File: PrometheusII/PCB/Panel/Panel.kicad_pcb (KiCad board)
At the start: 2 copper layers, 40.3 x 128.5 mm, 4 parts

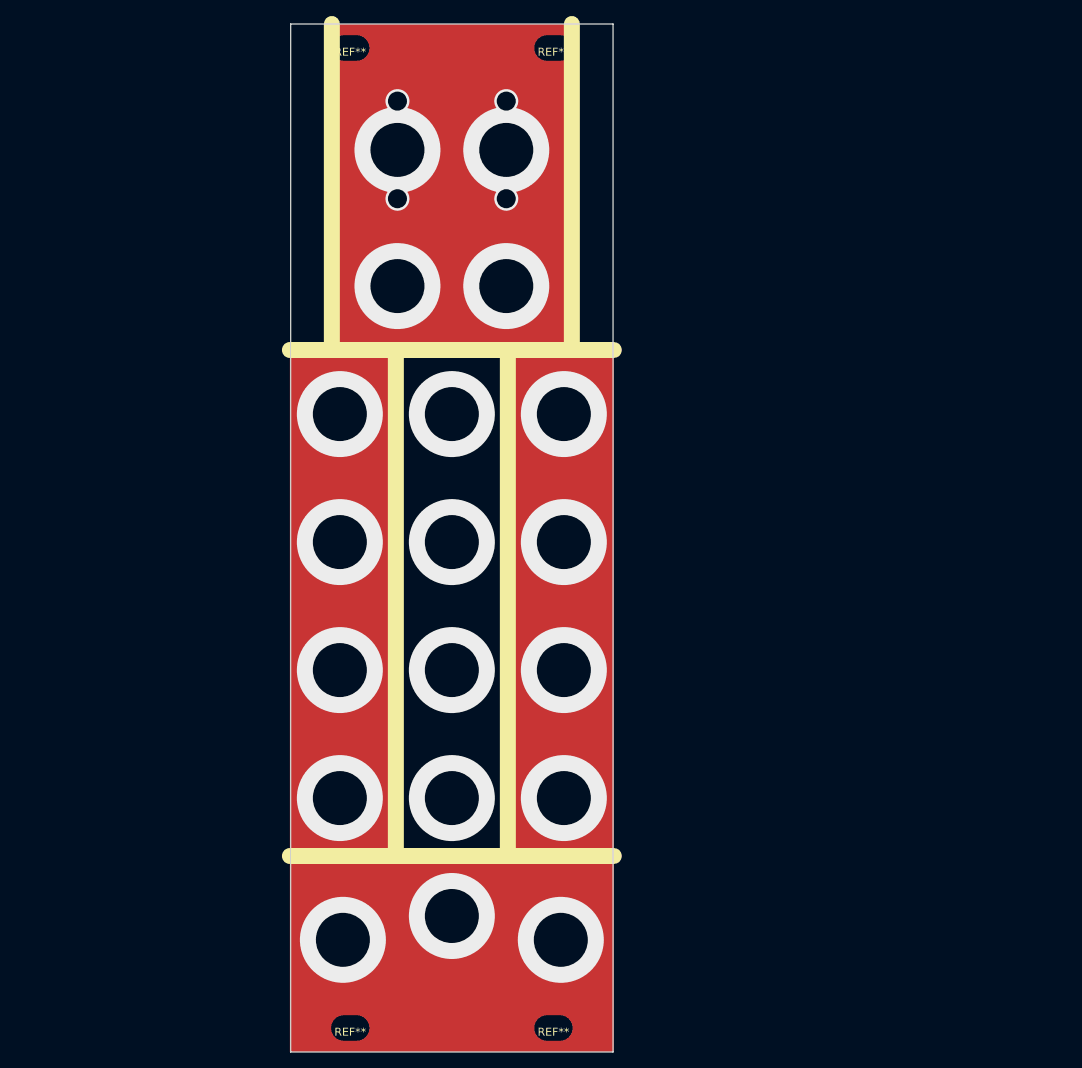
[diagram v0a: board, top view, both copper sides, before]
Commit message: Various DRC fixes
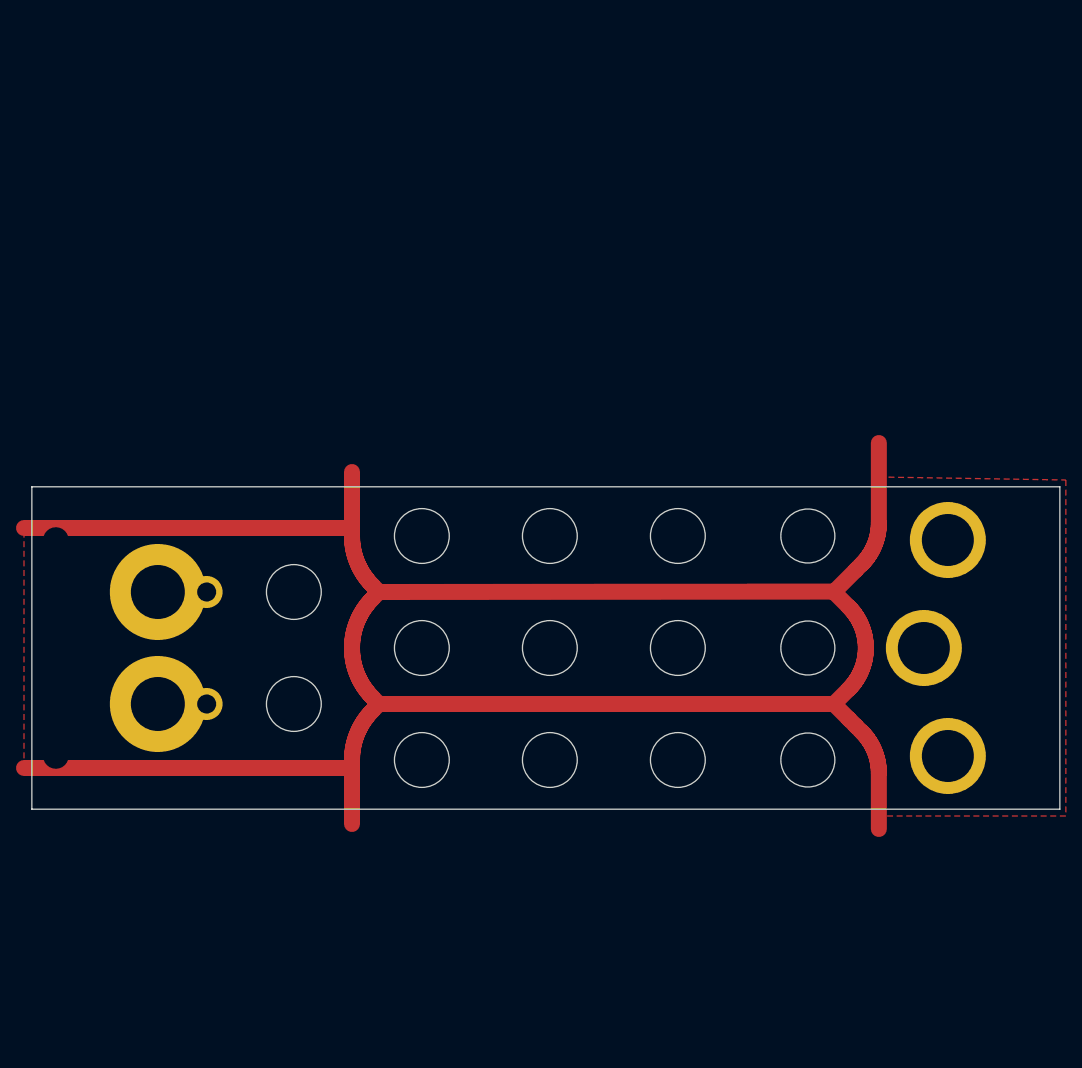
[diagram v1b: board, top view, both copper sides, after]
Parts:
- removed the REF** at (112.7, 24.5)
- removed the REF** at (87.3, 24.5)
- removed the REF** at (87.3, 147.0)
- removed the REF** at (112.7, 147.0)
- added G***: LOGO, ttt_lib:TTT_11.1x9.5, B.Cu at (74.5, 99.5)
- added REF**: PJ398SM_Plated, ttt_panels:PJ398SM_Plated, F.Cu at (162.0, 113.0)
- added REF**: Knob_Unplated, ttt_panels:Knob_Unplated, F.Cu at (112.2, 85.5)
- added REF**: Knob_Unplated, ttt_panels:Knob_Unplated, F.Cu at (112.2, 113.5)
- added REF**: Knob_Unplated, ttt_panels:Knob_Unplated, F.Cu at (112.2, 99.5)
- added REF**: Knob_Unplated, ttt_panels:Knob_Unplated, F.Cu at (96.2, 113.5)
- added REF**: Knob_Unplated, ttt_panels:Knob_Unplated, F.Cu at (96.2, 99.5)
- added REF**: Knob_Unplated, ttt_panels:Knob_Unplated, F.Cu at (80.2, 106.5)
- added REF**: Knob_Unplated, ttt_panels:Knob_Unplated, F.Cu at (80.2, 92.5)
- added REF**: Knob_Unplated, ttt_panels:Knob_Unplated, F.Cu at (96.2, 85.5)
- added REF**: Funswitch_Plated, ttt_panels:Funswitch_Plated, F.Cu at (63.2, 106.5)
- added REF**: Funswitch_Plated, ttt_panels:Funswitch_Plated, F.Cu at (63.2, 92.5)
- added REF**: PJ398SM_Unplated, ttt_panels:PJ398SM_Unplated, F.Cu at (144.5, 99.5)
- added REF**: euro_mounting_hole, ttt_lib:euro_mounting_hole, F.Cu at (173.0, 86.8)
- added REF**: euro_mounting_hole, ttt_lib:euro_mounting_hole, F.Cu at (173.0, 112.2)
- added REF**: euro_mounting_hole, ttt_lib:euro_mounting_hole, F.Cu at (50.5, 86.8)
- added REF**: PJ398SM_Plated, ttt_panels:PJ398SM_Plated, F.Cu at (162.0, 86.0)
- added REF**: euro_mounting_hole, ttt_lib:euro_mounting_hole, F.Cu at (50.5, 112.2)
- added REF**: PJ398SM_Unplated, ttt_panels:PJ398SM_Unplated, F.Cu at (144.5, 85.5)
- added REF**: Knob_Unplated, ttt_panels:Knob_Unplated, F.Cu at (128.2, 113.5)
- added REF**: Knob_Unplated, ttt_panels:Knob_Unplated, F.Cu at (128.2, 99.5)
- added REF**: Knob_Unplated, ttt_panels:Knob_Unplated, F.Cu at (128.2, 85.5)
- added REF**: PJ398SM_Unplated, ttt_panels:PJ398SM_Unplated, F.Cu at (144.5, 113.5)
- added REF**: PJ398SM_Plated, ttt_panels:PJ398SM_Plated, F.Cu at (159.0, 99.5)
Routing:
- net (no net): track 0.00 -> 298.9 mm, vias 23 -> 0
- added copper zone on F.Cu, net (none)
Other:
- board size 40.3 x 128.5 mm -> 128.5 x 40.3 mm
- board text added: "2020-07"
- board text added: "JLCJLCJLCJLC"
- board text added: "Prometheus II Rev 01"
